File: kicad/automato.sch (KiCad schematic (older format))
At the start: 68 parts, among them J1 USB_C_Receptacle, J2 LiPo, J3 Conn_01x07_Male, J4 Screw_Terminal_01x20, J5 USB_C_Receptacle, J8 Micro_SD_Card_Det, M1 eink-module, Q1 Q_NPN_BCE, Q2 Q_NPN_BCE, Q3 DMG3415U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

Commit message: add sma
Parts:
- added J6: Conn_Coaxial, Connector_Coaxial:SMA_Wurth_60312002114503_Vertical, symbol Connector:Conn_Coaxial
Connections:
- net GND: now also J6.2 (Ext)
- net at AE1.1 (A), U3.9 (ANT): now also J6.1 (In)
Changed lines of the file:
@@
 Text GLabel 9500 9050 1    50   Input ~ 0
 IO15
+$Comp
+L Connector:Conn_Coaxial J6
+U 1 1 63230F63
+P 16150 5850
+F 0 "J6" H 16250 5825 50  0000 L CNN
+F 1 "Conn_Coaxial" H 16250 5734 50  0000 L CNN
+F 2 "Connector_Coaxial:SMA_Wurth_60312002114503_Vertical" H 16150 5850 50  0001 C CNN
+F 3 " ~" H 16150 5850 50  0001 C CNN
+	1    16150 5850
+	1    0    0    -1
+$EndComp
+Wire Wire Line
+	15600 5850 15950 5850
+Connection ~ 15600 5850
+$Comp
+L power:GND #PWR?
+U 1 1 63249D3B
+P 16150 6050
+F 0 "#PWR?" H 16150 5800 50  0001 C CNN
+F 1 "GND" H 16155 5877 50  0000 C CNN
+F 2 "" H 16150 6050 50  0001 C CNN
+F 3 "" H 16150 6050 50  0001 C CNN
+	1    16150 6050
+	1    0    0    -1
+$EndComp
 $EndSCHEMATC

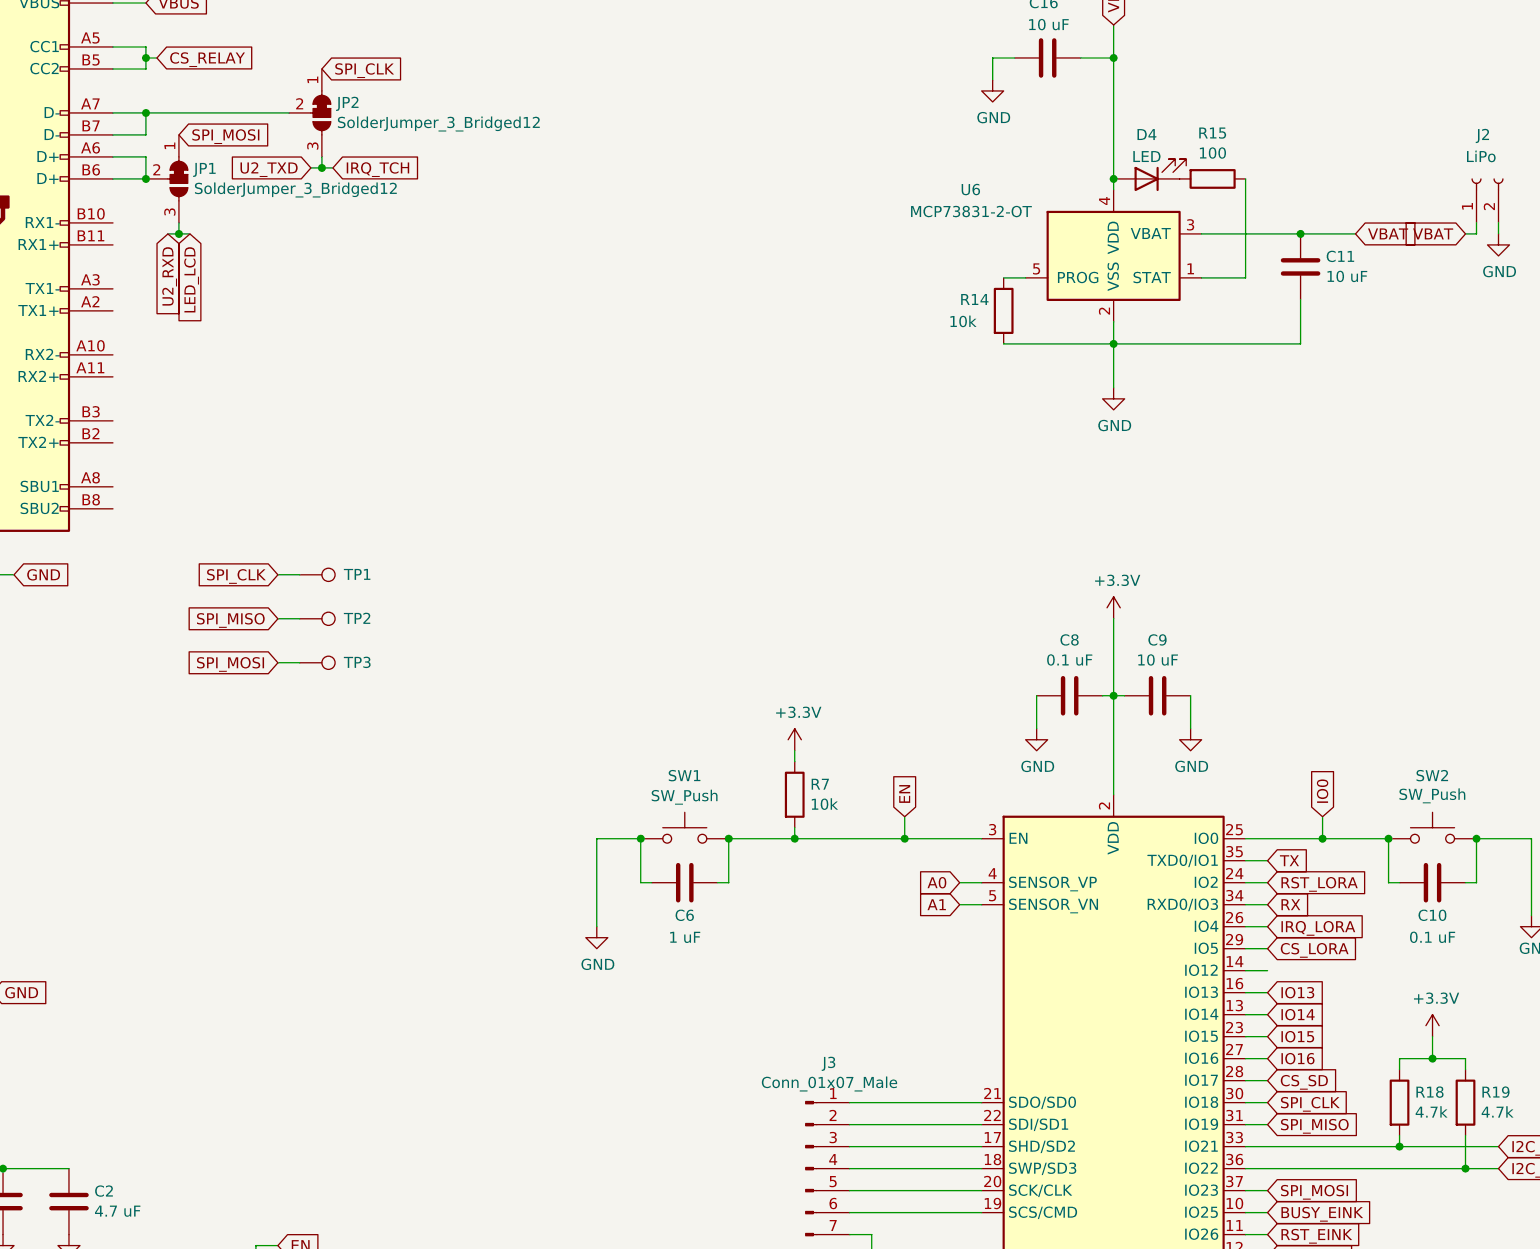
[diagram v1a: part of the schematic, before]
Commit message: swapped cs_sd and cs_relay pins
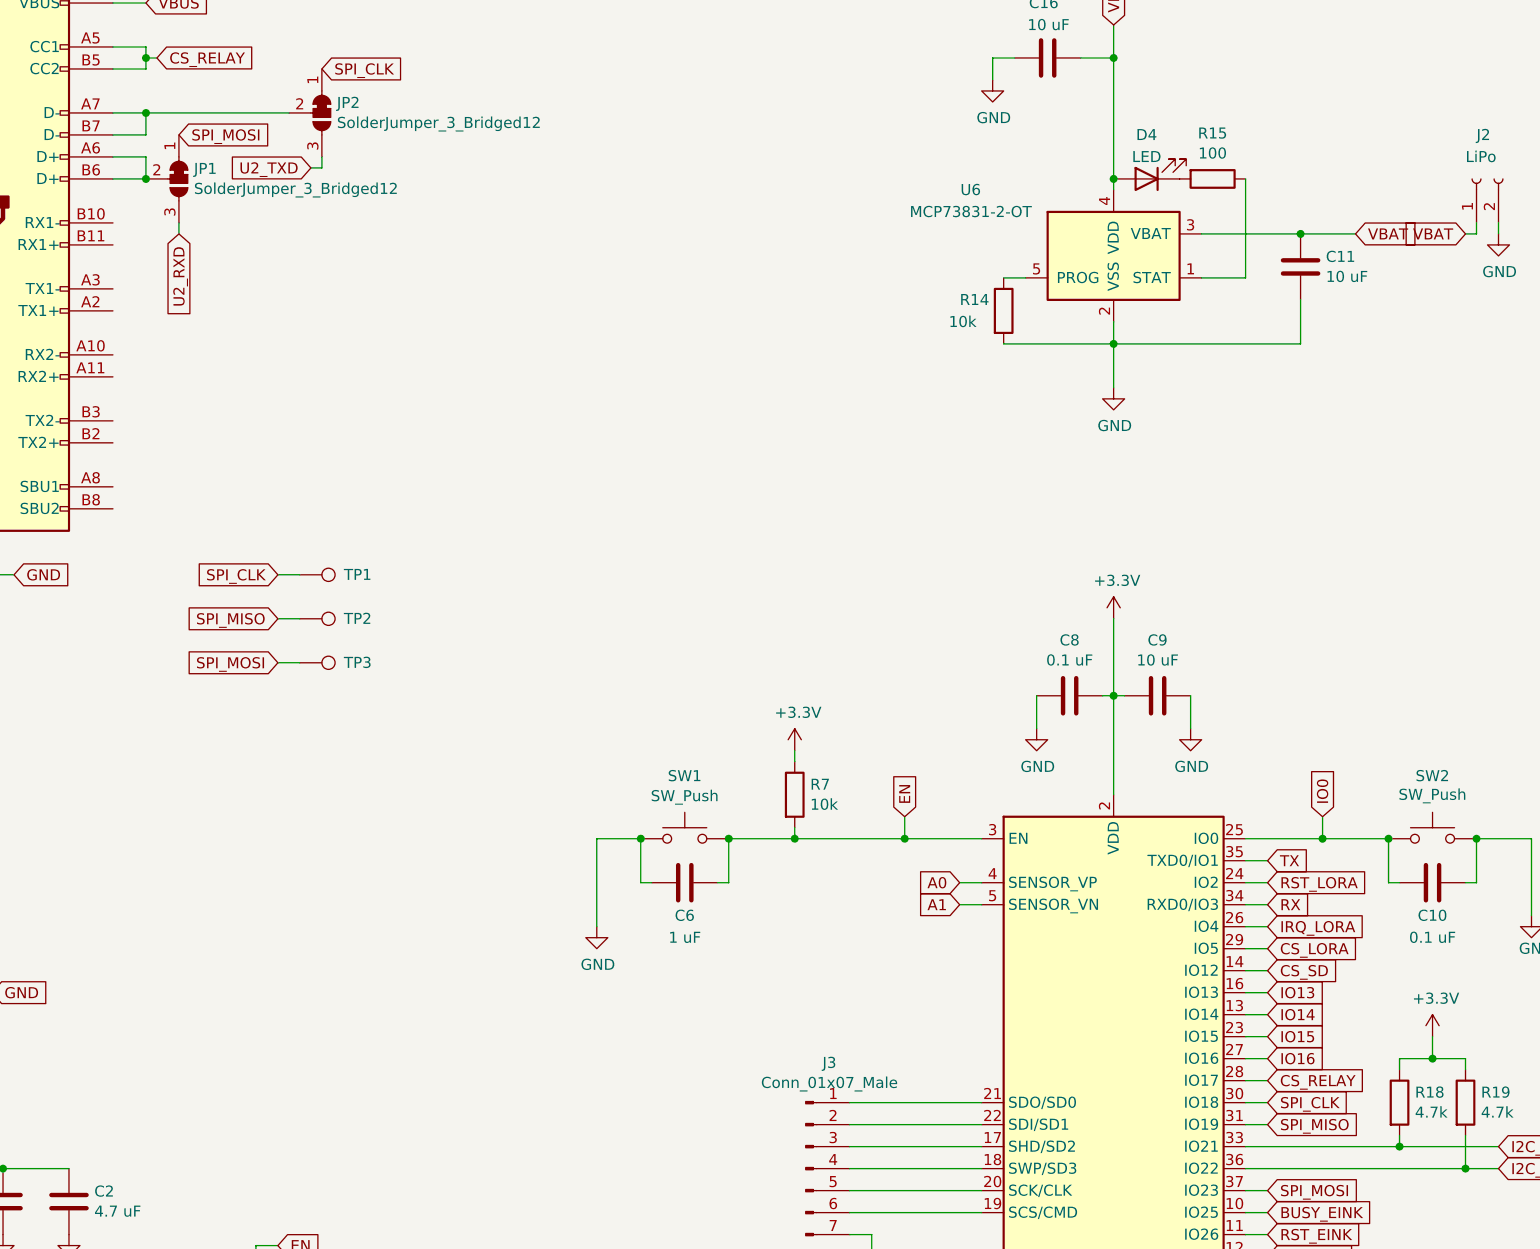
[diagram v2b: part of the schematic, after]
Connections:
- net CS_RELAY: now also U4.28 (IO17)
- net CS_SD: now also U4.14 (IO12); no longer U4.28 (IO17)
- net IRQ_TCH renamed U2_TXD
- net LED_LCD renamed U2_RXD
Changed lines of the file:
@@
 Wire Wire Line
 	9550 5350 9650 5350
-Text GLabel 9650 5850 2    50   Input ~ 0
+Text GLabel 9650 5350 2    50   Input ~ 0
 CS_SD
 Text GLabel 9650 5950 2    50   Input ~ 0
@@
 	4550 1450 5200 1450
 Connection ~ 4550 1450
-Text GLabel 4750 2000 3    50   Input ~ 0
-LED_LCD
-Text GLabel 5400 1700 2    50   Input ~ 0
-IRQ_TCH
 Text GLabel 5300 1700 0    50   Input ~ 0
 U2_TXD
-Text GLabel 4650 2000 3    50   Input ~ 0
+Text GLabel 4700 2000 3    50   Input ~ 0
 U2_RXD
 Wire Wire Line
 	4700 1950 4700 2000
 Wire Wire Line
-	4700 2000 4750 2000
-Wire Wire Line
 	5350 1650 5350 1700
 Wire Wire Line
 	5350 1700 5300 1700
-Wire Wire Line
-	5400 1700 5350 1700
-Connection ~ 5350 1700
-Wire Wire Line
-	4650 2000 4700 2000
-Connection ~ 4700 2000
 Wire Wire Line
 	2050 4650 1850 4650
@@
 Connection ~ 15600 5850
 $Comp
-L power:GND #PWR?
+L power:GND #PWR0104
 U 1 1 63249D3B
 P 16150 6050
-F 0 "#PWR?" H 16150 5800 50  0001 C CNN
+F 0 "#PWR0104" H 16150 5800 50  0001 C CNN
 F 1 "GND" H 16155 5877 50  0000 C CNN
 F 2 "" H 16150 6050 50  0001 C CNN
@@
 	1    0    0    -1
 $EndComp
+Text GLabel 9650 5850 2    50   Input ~ 0
+CS_RELAY
 $EndSCHEMATC

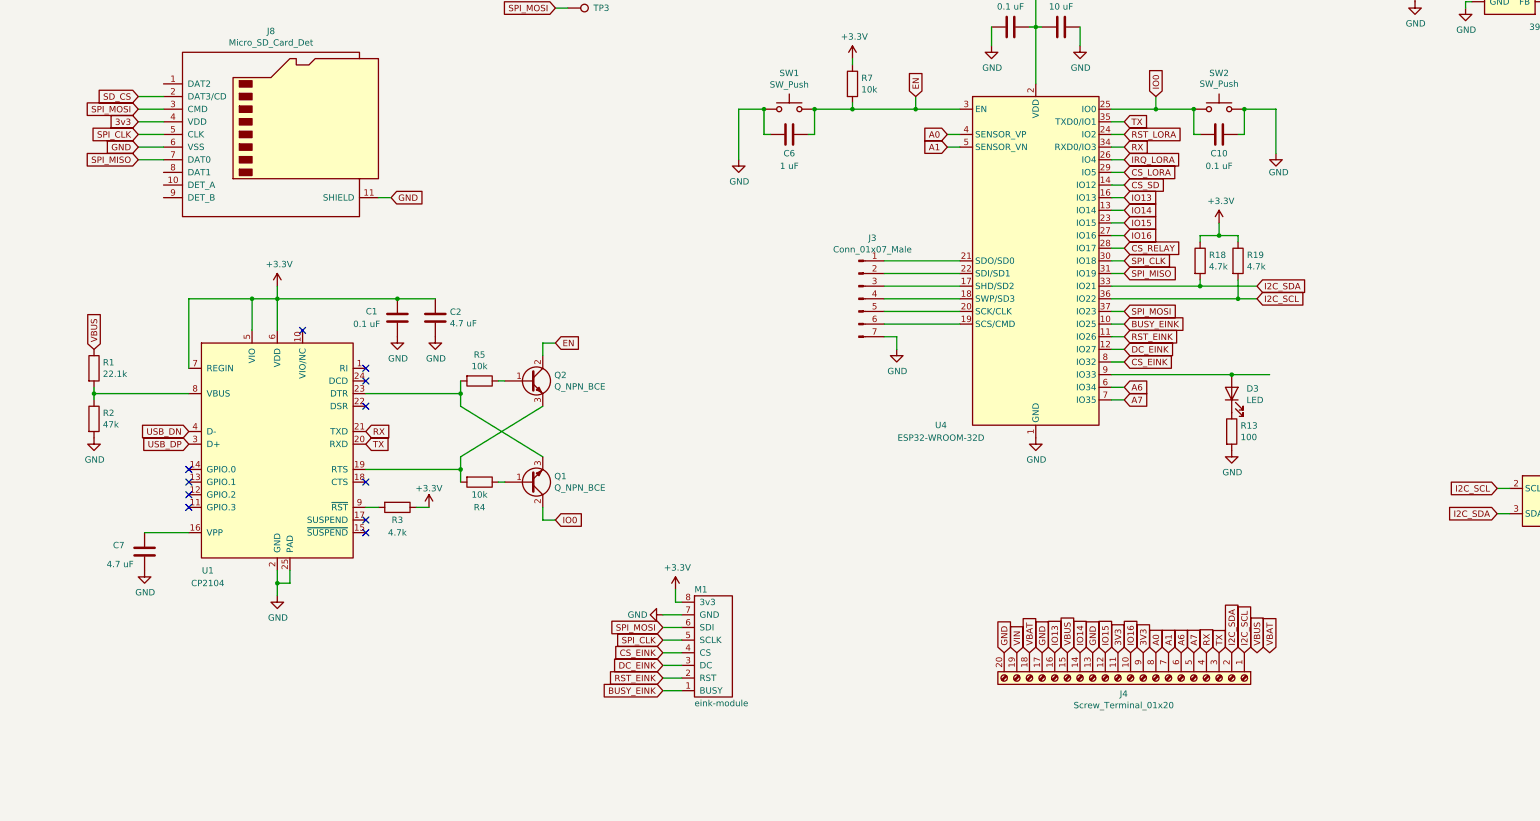
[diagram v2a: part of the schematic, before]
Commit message: add qwiic, i2c, 1wire jst
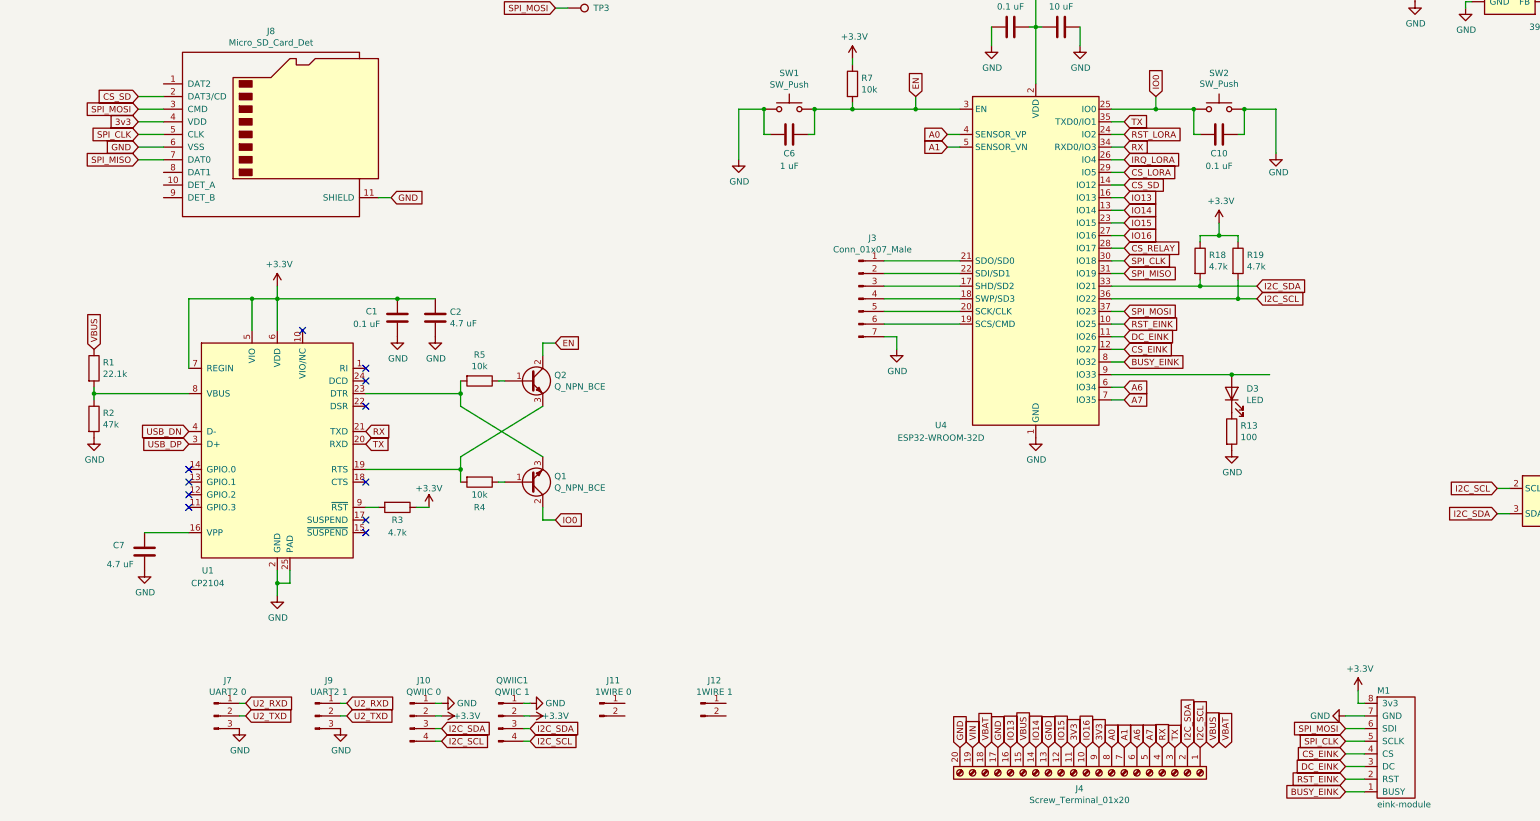
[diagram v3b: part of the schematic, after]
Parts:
- added J10: QWIIC 0, Connector_JST:JST_SH_SM04B-SRSS-TB_1x04-1MP_P1.00mm_Horizontal, symbol Connector:Conn_01x04_Male
- added J11: 1WIRE 0, symbol Connector:Conn_01x02_Male
- added J12: 1WIRE 1, symbol Connector:Conn_01x02_Male
- added J7: UART2 0, symbol Connector:Conn_01x03_Male
- added J9: UART2 1, symbol Connector:Conn_01x03_Male
- added QWIIC1: QWIIC 1, Connector_JST:JST_SH_SM04B-SRSS-TB_1x04-1MP_P1.00mm_Horizontal, symbol Connector:Conn_01x04_Male
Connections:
- net SD_CS is gone; now on net CS_SD: J8.2 (DAT3/CD)
- net +3V3: now also J10.2 (Pin_2), QWIIC1.2 (Pin_2)
- net BUSY_EINK: now also U4.8 (IO32); no longer U4.10 (IO25)
- net CS_EINK: now also U4.12 (IO27); no longer U4.8 (IO32)
- net DC_EINK: now also U4.11 (IO26); no longer U4.12 (IO27)
- net GND: now also J10.1 (Pin_1), J7.3 (Pin_3), J9.3 (Pin_3), QWIIC1.1 (Pin_1)
- net I2C_SCL: now also J10.4 (Pin_4), QWIIC1.4 (Pin_4)
- net I2C_SDA: now also J10.3 (Pin_3), QWIIC1.3 (Pin_3)
- net RST_EINK: now also U4.10 (IO25); no longer U4.11 (IO26)
- net U2_RXD: now also J7.1 (Pin_1), J9.1 (Pin_1)
- net U2_TXD: now also J7.2 (Pin_2), J9.2 (Pin_2)
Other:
- moved on the sheet: J4, M1
